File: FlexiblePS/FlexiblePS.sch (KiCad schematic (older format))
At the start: 118 parts, among them J1 Conn_01x02, J10 Conn_01x01, J11 Conn_01x01, J12 Conn_01x04, J13 Conn_01x02, J14 Conn_01x02, J15 Conn_01x02, J2 Conn_02x03_Odd_Even, J3 Conn_01x02, J4 Conn_01x02, J5 Conn_01x02, J6 Conn_01x01, J7 Conn_01x01, J8 Conn_01x02, J9 Conn_01x02, Q1 TIP42, Q2 TIP41, Q3 2N3906, Q4 TIP41C, U1 ATMEGA328P-PU, U2 LM358, U3 LCD-016N002L, U4 TL494, U5 LMT85, U6 LMT85, U9 LM7805_TO220, X3 16MHz

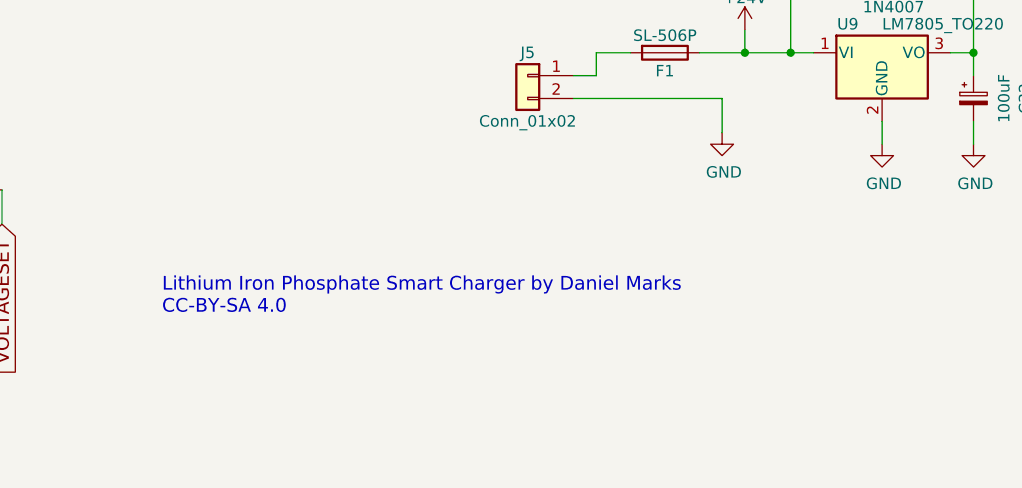
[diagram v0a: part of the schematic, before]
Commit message: Renamed project to FlexiblePS
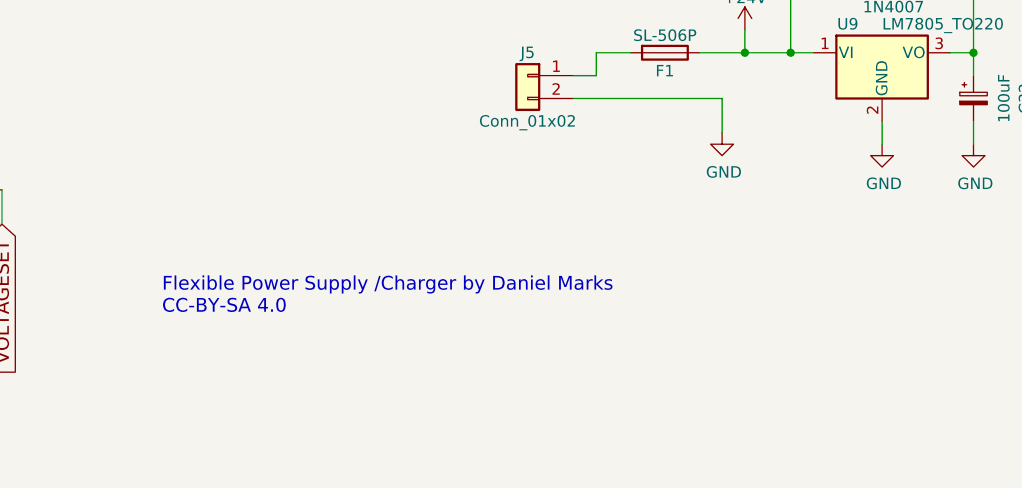
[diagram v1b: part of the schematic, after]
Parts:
- F1: footprint LiFePO4smartcharger:SL506Pfuseholder -> FlexiblePS:SL506Pfuseholder
- Q2: footprint LiFePO4smartcharger:TO-247_TO-3P_Vertical -> FlexiblePS:TO-247_TO-3P_Vertical
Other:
- note added: "Flexible Power Supply /Charger by Daniel Marks\nCC-BY-SA 4.0"
- note removed: "Lithium Iron Phosphate Smart Charger by Daniel Marks\nCC-BY-SA 4.0"
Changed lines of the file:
@@
 EESchema Schematic File Version 2
-LIBS:LiFePO4SmartCharger-rescue
+LIBS:FlexiblePS-rescue
 LIBS:power
 LIBS:device
@@
 LIBS:tl494
 LIBS:lm35
-LIBS:LiFePO4smartcharger-cache
+LIBS:FlexiblePS-cache
 EELAYER 25 0
 EELAYER END
@@
 $EndComp
 Text Notes 7350 6950 0    60   ~ 0
-Lithium Iron Phosphate Smart Charger by Daniel Marks\nCC-BY-SA 4.0
+Flexible Power Supply /Charger by Daniel Marks\nCC-BY-SA 4.0
 $Comp
 L C C19
@@
 F 0 "F1" V 9630 5800 50  0000 C CNN
 F 1 "SL-506P" V 9475 5800 50  0000 C CNN
-F 2 "LiFePO4smartcharger:SL506Pfuseholder" V 9480 5800 50  0001 C CNN
+F 2 "FlexiblePS:SL506Pfuseholder" V 9480 5800 50  0001 C CNN
 F 3 "" H 9550 5800 50  0001 C CNN
 	1    9550 5800
@@
 F 0 "Q2" V 5000 4750 50  0000 L CNN
 F 1 "TIP41" V 4900 4700 50  0000 L CNN
-F 2 "LiFePO4smartcharger:TO-247_TO-3P_Vertical" H 4950 4725 50  0001 L CIN
+F 2 "FlexiblePS:TO-247_TO-3P_Vertical" H 4950 4725 50  0001 L CIN
 F 3 "" H 4700 4800 50  0001 L CNN
 	1    4700 4800
